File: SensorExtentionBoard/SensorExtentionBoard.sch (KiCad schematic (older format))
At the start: 27 parts, among them J1 Conn_01x02_Male, J2 Conn_01x02_Male, J3 Conn_02x03_Top_Bottom, J4 Conn_01x02_Male, J5 Conn_01x05_Male, U1 TCA9544A, U2 TCA9555DBR

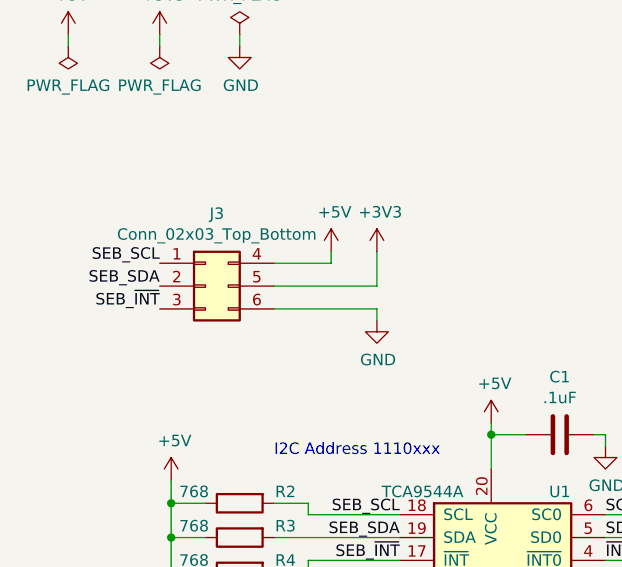
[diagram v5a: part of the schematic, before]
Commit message: Changed component footprints to conform to RP standard components
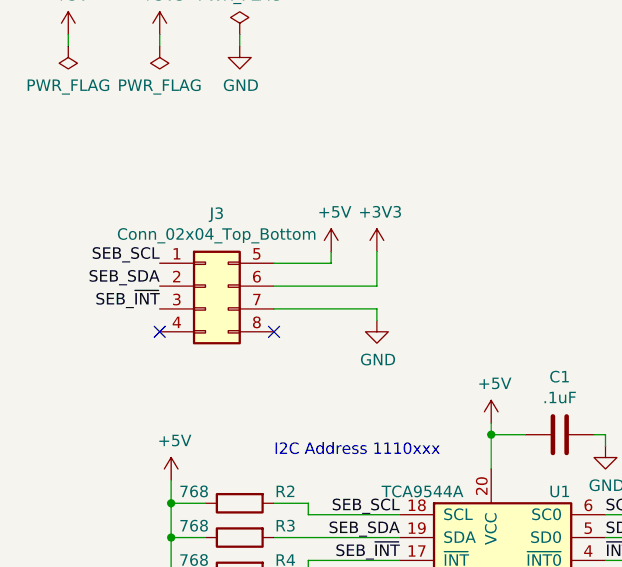
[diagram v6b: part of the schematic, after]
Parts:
- removed J3: Conn_02x03_Top_Bottom, Connector_Molex:Molex_Micro-Fit_3.0_43045-0612_2x03_P3.00mm_Vertical, symbol Connector_Generic:Conn_02x03_Top_Bottom
- added J3: Conn_02x04_Top_Bottom, Connector_Molex:Molex_Micro-Fit_3.0_43045-0800_2x04_P3.00mm_Horizontal, symbol Connector_Generic:Conn_02x04_Top_Bottom
- C1, C2: footprint (none) -> Capacitor_SMD:C_1206_3216Metric_Pad1.42x1.75mm_HandSolder
- J5: footprint Connector_Molex:Molex_MicroClasp_55932-0510_1x05_P2.00mm_Vertical -> Connector_Molex:Molex_MicroClasp_55932-0530_1x05_P2.00mm_Vertical
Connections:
- net +3V3: now also J3.6 (Pin_6)
- net +5V: now also J3.5 (Pin_5)
- net GND: now also J3.7 (Pin_7)
- net SEB_SCL: now also J3.1 (Pin_1)
- net SEB_SDA: now also J3.2 (Pin_2)
- net SEB_~INT: now also J3.3 (Pin_3)
- no-connect marks 6 -> 8
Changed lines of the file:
@@
 encoding utf-8
 Sheet 1 5
-Title ""
-Date ""
-Rev ""
-Comp ""
-Comment1 ""
+Title "Helix Test Rig SEB"
+Date "2020-01-14"
+Rev "1.0.0"
+Comp "SDSU Rocket Project"
+Comment1 "Schematic Design: David Knight"
 Comment2 ""
 Comment3 ""
@@
 SEB_SDA
 $Comp
-L power:GND #PWR011
+L power:GND #PWR014
 U 1 1 5E40560B
 P 2550 4550
-F 0 "#PWR011" H 2550 4300 50  0001 C CNN
+F 0 "#PWR014" H 2550 4300 50  0001 C CNN
 F 1 "GND" H 2555 4377 50  0000 C CNN
 F 2 "" H 2550 4550 50  0001 C CNN
@@
 	2550 4550 2550 4500
 $Comp
-L power:+5V #PWR010
+L power:+5V #PWR013
 U 1 1 5E4066C5
 P 2550 2400
-F 0 "#PWR010" H 2550 2250 50  0001 C CNN
+F 0 "#PWR013" H 2550 2250 50  0001 C CNN
 F 1 "+5V" H 2565 2573 50  0000 C CNN
 F 2 "" H 2550 2400 50  0001 C CNN
@@
 SEB_SDA
 $Comp
-L power:+5V #PWR06
+L power:+5V #PWR09
 U 1 1 5E40BD65
 P 1850 1650
-F 0 "#PWR06" H 1850 1500 50  0001 C CNN
+F 0 "#PWR09" H 1850 1500 50  0001 C CNN
 F 1 "+5V" H 1865 1823 50  0000 C CNN
 F 2 "" H 1850 1650 50  0001 C CNN
@@
 	4750 1000 7200 1000
 $Comp
-L power:GND #PWR02
+L power:GND #PWR03
 U 1 1 5E4557E3
 P 1050 4650
-F 0 "#PWR02" H 1050 4400 50  0001 C CNN
+F 0 "#PWR03" H 1050 4400 50  0001 C CNN
 F 1 "GND" H 1055 4477 50  0000 C CNN
 F 2 "" H 1050 4650 50  0001 C CNN
@@
 	2000 4600 2000 4550
 $Comp
-L power:+5V #PWR07
+L power:+5V #PWR010
 U 1 1 5E478158
 P 2000 3750
-F 0 "#PWR07" H 2000 3600 50  0001 C CNN
+F 0 "#PWR010" H 2000 3600 50  0001 C CNN
 F 1 "+5V" H 2015 3923 50  0000 C CNN
 F 2 "" H 2000 3750 50  0001 C CNN
@@
 $EndComp
 $Comp
-L power:+5V #PWR04
+L power:+5V #PWR07
 U 1 1 5E47880F
 P 1500 3750
-F 0 "#PWR04" H 1500 3600 50  0001 C CNN
+F 0 "#PWR07" H 1500 3600 50  0001 C CNN
 F 1 "+5V" H 1515 3923 50  0000 C CNN
 F 2 "" H 1500 3750 50  0001 C CNN
@@
 $EndComp
 $Comp
-L power:+5V #PWR01
+L power:+5V #PWR02
 U 1 1 5E478B23
 P 1050 3750
-F 0 "#PWR01" H 1050 3600 50  0001 C CNN
+F 0 "#PWR02" H 1050 3600 50  0001 C CNN
 F 1 "+5V" H 1065 3923 50  0000 C CNN
 F 2 "" H 1050 3750 50  0001 C CNN
@@
 $EndComp
 $Comp
-L power:GND #PWR013
+L power:GND #PWR016
 U 1 1 5E4B55BB
 P 2550 7400
-F 0 "#PWR013" H 2550 7150 50  0001 C CNN
+F 0 "#PWR016" H 2550 7150 50  0001 C CNN
 F 1 "GND" H 2555 7227 50  0000 C CNN
 F 2 "" H 2550 7400 50  0001 C CNN
@@
 	2550 7400 2550 7350
 $Comp
-L power:+5V #PWR012
+L power:+5V #PWR015
 U 1 1 5E4B8530
 P 2550 5000
-F 0 "#PWR012" H 2550 4850 50  0001 C CNN
+F 0 "#PWR015" H 2550 4850 50  0001 C CNN
 F 1 "+5V" H 2565 5173 50  0000 C CNN
 F 2 "" H 2550 5000 50  0001 C CNN
@@
 ~INT3
 $Comp
-L power:GND #PWR05
+L power:GND #PWR08
 U 1 1 5E4F4899
 P 1800 7100
-F 0 "#PWR05" H 1800 6850 50  0001 C CNN
+F 0 "#PWR08" H 1800 6850 50  0001 C CNN
 F 1 "GND" H 1805 6927 50  0000 C CNN
 F 2 "" H 1800 7100 50  0001 C CNN
@@
 	4050 2900 4050 2750
 $Comp
-L power:+5V #PWR016
+L power:+5V #PWR019
 U 1 1 5E54BF49
 P 4050 2650
-F 0 "#PWR016" H 4050 2500 50  0001 C CNN
+F 0 "#PWR019" H 4050 2500 50  0001 C CNN
 F 1 "+5V" H 4065 2823 50  0000 C CNN
 F 2 "" H 4050 2650 50  0001 C CNN
@@
 	1150 2650 1150 2750
 $Comp
-L power:+5V #PWR03
+L power:+5V #PWR05
 U 1 1 5E56EC2F
 P 1150 2650
-F 0 "#PWR03" H 1150 2500 50  0001 C CNN
+F 0 "#PWR05" H 1150 2500 50  0001 C CNN
 F 1 "+5V" H 1165 2823 50  0000 C CNN
 F 2 "" H 1150 2650 50  0001 C CNN
@@
 F 0 "C1" V 2598 2450 50  0000 C CNN
 F 1 ".1uF" V 2689 2450 50  0000 C CNN
-F 2 "" H 2888 2300 50  0001 C CNN
+F 2 "Capacitor_SMD:C_1206_3216Metric_Pad1.42x1.75mm_HandSolder" H 2888 2300 50  0001 C CNN
 F 3 "~" H 2850 2450 50  0001 C CNN
 	1    2850 2450
@@
 $EndComp
 $Comp
-L power:GND #PWR014
+L power:GND #PWR017
 U 1 1 5E10FBD2
 P 3050 2500
-F 0 "#PWR014" H 3050 2250 50  0001 C CNN
+F 0 "#PWR017" H 3050 2250 50  0001 C CNN
 F 1 "GND" H 3055 2327 50  0000 C CNN
 F 2 "" H 3050 2500 50  0001 C CNN
@@
 F 0 "C2" V 2698 5050 50  0000 C CNN
 F 1 ".1uF" V 2789 5050 50  0000 C CNN
-F 2 "" H 2988 4900 50  0001 C CNN
+F 2 "Capacitor_SMD:C_1206_3216Metric_Pad1.42x1.75mm_HandSolder" H 2988 4900 50  0001 C CNN
 F 3 "~" H 2950 5050 50  0001 C CNN
 	1    2950 5050
@@
 $EndComp
 $Comp
-L power:GND #PWR015
+L power:GND #PWR018
 U 1 1 5E12739C
 P 3150 5100
-F 0 "#PWR015" H 3150 4850 50  0001 C CNN
+F 0 "#PWR018" H 3150 4850 50  0001 C CNN
 F 1 "GND" H 3155 4927 50  0000 C CNN
 F 2 "" H 3150 5100 50  0001 C CNN
@@
 F 0 "J5" H 5058 7231 50  0000 C CNN
 F 1 "Conn_01x05_Male" H 5058 7140 50  0000 C CNN
-F 2 "Connector_Molex:Molex_MicroClasp_55932-0510_1x05_P2.00mm_Vertical" H 4950 6850 50  0001 C CNN
+F 2 "Connector_Molex:Molex_MicroClasp_55932-0530_1x05_P2.00mm_Vertical" H 4950 6850 50  0001 C CNN
 F 3 "~" H 4950 6850 50  0001 C CNN
 	1    4950 6850
@@
 $EndComp
 $Comp
-L power:+3V3 #PWR08
+L power:+3V3 #PWR011
 U 1 1 5E1E7AA4
 P 2050 1650
-F 0 "#PWR08" H 2050 1500 50  0001 C CNN
+F 0 "#PWR011" H 2050 1500 50  0001 C CNN
 F 1 "+3V3" H 2065 1823 50  0000 C CNN
 F 2 "" H 2050 1650 50  0001 C CNN
@@
 	2050 1800 2050 1650
 $Comp
-L Connector_Generic:Conn_02x03_Top_Bottom J3
-U 1 1 5E40940C
-P 1300 1800
-F 0 "J3" H 1350 2117 50  0000 C CNN
-F 1 "Conn_02x03_Top_Bottom" H 1350 2026 50  0000 C CNN
-F 2 "Connector_Molex:Molex_Micro-Fit_3.0_43045-0612_2x03_P3.00mm_Vertical" H 1300 1800 50  0001 C CNN
-F 3 "~" H 1300 1800 50  0001 C CNN
-	1    1300 1800
-	1    0    0    -1
-$EndComp
-$Comp
-L power:GND #PWR09
+L power:GND #PWR012
 U 1 1 5E1FD07B
 P 2050 1950
-F 0 "#PWR09" H 2050 1700 50  0001 C CNN
+F 0 "#PWR012" H 2050 1700 50  0001 C CNN
 F 1 "GND" H 2055 1777 50  0000 C CNN
 F 2 "" H 2050 1950 50  0001 C CNN
@@
 	2050 1900 2050 1950
 $Comp
-L power:+3V3 #PWR017
+L power:+3V3 #PWR020
 U 1 1 5E208288
 P 5450 6600
-F 0 "#PWR017" H 5450 6450 50  0001 C CNN
+F 0 "#PWR020" H 5450 6450 50  0001 C CNN
 F 1 "+3V3" H 5465 6773 50  0000 C CNN
 F 2 "" H 5450 6600 50  0001 C CNN
@@
 SDA3
 $Comp
-L power:GND #PWR018
+L power:GND #PWR021
 U 1 1 5E219BB3
 P 5800 7050
-F 0 "#PWR018" H 5800 6800 50  0001 C CNN
+F 0 "#PWR021" H 5800 6800 50  0001 C CNN
 F 1 "GND" H 5805 6877 50  0000 C CNN
 F 2 "" H 5800 7050 50  0001 C CNN
@@
 	5150 6950 5800 6950
 $Comp
-L power:PWR_FLAG #FLG0101
+L power:PWR_FLAG #FLG01
 U 1 1 5E237C05
 P 700 750
-F 0 "#FLG0101" H 700 825 50  0001 C CNN
+F 0 "#FLG01" H 700 825 50  0001 C CNN
 F 1 "PWR_FLAG" H 700 923 50  0000 C CNN
 F 2 "" H 700 750 50  0001 C CNN
@@
 $EndComp
 $Comp
-L power:PWR_FLAG #FLG0102
+L power:PWR_FLAG #FLG02
 U 1 1 5E2383B9
 P 1100 750
-F 0 "#FLG0102" H 1100 825 50  0001 C CNN
+F 0 "#FLG02" H 1100 825 50  0001 C CNN
 F 1 "PWR_FLAG" H 1100 923 50  0000 C CNN
 F 2 "" H 1100 750 50  0001 C CNN
@@
 $EndComp
 $Comp
-L power:PWR_FLAG #FLG0103
+L power:PWR_FLAG #FLG03
 U 1 1 5E24BEC8
 P 1450 700
-F 0 "#FLG0103" H 1450 775 50  0001 C CNN
+F 0 "#FLG03" H 1450 775 50  0001 C CNN
 F 1 "PWR_FLAG" H 1450 873 50  0000 C CNN
 F 2 "" H 1450 700 50  0001 C CNN
@@
 $EndComp
 $Comp
-L power:+5V #PWR0101
+L power:+5V #PWR01
 U 1 1 5E24C057
 P 700 700
-F 0 "#PWR0101" H 700 550 50  0001 C CNN
+F 0 "#PWR01" H 700 550 50  0001 C CNN
 F 1 "+5V" H 715 873 50  0000 C CNN
 F 2 "" H 700 700 50  0001 C CNN
@@
 $EndComp
 $Comp
-L power:+3V3 #PWR0102
+L power:+3V3 #PWR04
 U 1 1 5E24C491
 P 1100 700
-F 0 "#PWR0102" H 1100 550 50  0001 C CNN
+F 0 "#PWR04" H 1100 550 50  0001 C CNN
 F 1 "+3V3" H 1115 873 50  0000 C CNN
 F 2 "" H 1100 700 50  0001 C CNN
@@
 	1100 700  1100 750
 $Comp
-L power:GND #PWR0103
+L power:GND #PWR06
 U 1 1 5E25AEE7
 P 1450 750
-F 0 "#PWR0103" H 1450 500 50  0001 C CNN
+F 0 "#PWR06" H 1450 500 50  0001 C CNN
 F 1 "GND" H 1455 577 50  0000 C CNN
 F 2 "" H 1450 750 50  0001 C CNN
@@
 Text Notes 6150 1800 0    50   ~ 0
 1010000
+$Comp
+L Connector_Generic:Conn_02x04_Top_Bottom J3
+U 1 1 5E1E8CCE
+P 1300 1800
+F 0 "J3" H 1350 2117 50  0000 C CNN
+F 1 "Conn_02x04_Top_Bottom" H 1350 2026 50  0000 C CNN
+F 2 "Connector_Molex:Molex_Micro-Fit_3.0_43045-0800_2x04_P3.00mm_Horizontal" H 1300 1800 50  0001 C CNN
+F 3 "~" H 1300 1800 50  0001 C CNN
+	1    1300 1800
+	1    0    0    -1
+$EndComp
+NoConn ~ 1600 2000
+NoConn ~ 1100 2000
 $EndSCHEMATC
